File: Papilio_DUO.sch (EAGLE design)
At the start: 110 parts, among them IC1 FT2232H, SW1 SWITCH-2CH-6P-3010010P1, SW2 EVQQ2, U1 ARDUINO_MEGA_SHIELD, U101 ATMEGA32U4-XUMU, U2 LTC3419EMS, U3 93C46B, X1 12MHz, Y1 16MHz KX-7

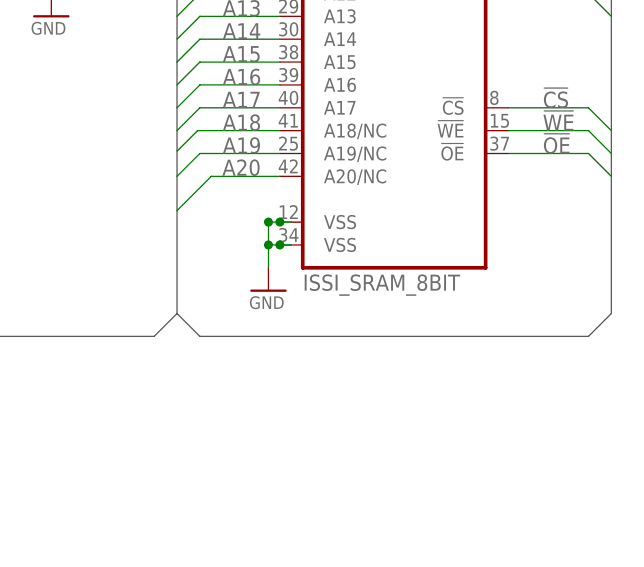
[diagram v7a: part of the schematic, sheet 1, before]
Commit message: Papilio DUO V1.4
Fixed the mounting holes.
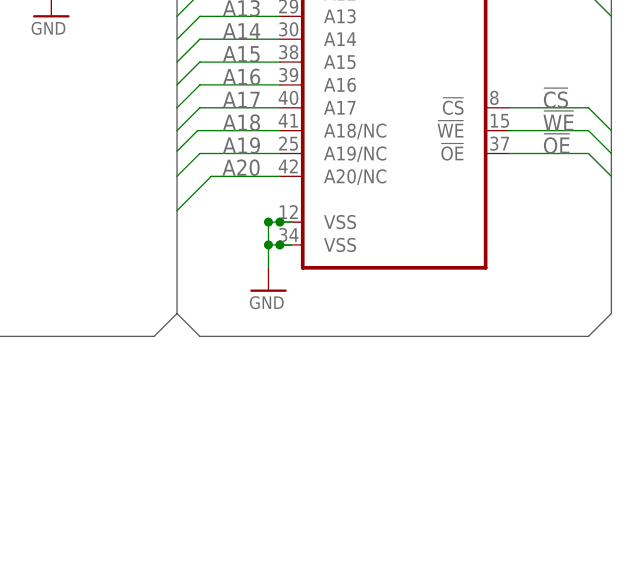
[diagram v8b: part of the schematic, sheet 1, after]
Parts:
- SRAM: value ISSI_SRAM_8BIT -> (none)
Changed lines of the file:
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@@
 </attributes>
 <variantdefs>
+<variantdef name="512KB-SRAM"/>
+<variantdef name="1MB-SRAM"/>
+<variantdef name="2MB-SRAM"/>
+<variantdef name="No-SRAM"/>
 </variantdefs>
 <classes>
@@
 <part name="SRAM" library="GadgetFactory" deviceset="ISSI_SRAM_8BIT" device="">
 <attribute name="PARTNO" value="IS61WV20488BLL-10TLI"/>
+<variant name="512KB-SRAM" value="512KB-SRAM"/>
+<variant name="1MB-SRAM" value="1MB-SRAM"/>
+<variant name="2MB-SRAM" value="2MB-SRAM"/>
+<variant name="No-SRAM" populate="no"/>
 </part>
 <part name="GND4" library="supply1" deviceset="GND" device=""/>
